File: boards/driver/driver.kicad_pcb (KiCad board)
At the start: 6 copper layers, 228.6 x 110.7 mm, 687 parts, among them J1 DIN41612_03x32_C, J2 Barrel_Jack_Switch, J3 Conn_01x24, J4 Conn_01x24, Q1 MMBT2222, Q10 MMBT2222, Q11 MMBT2222, Q12 MMBT2222, Q13 MMBT2222, Q14 MMBT2222, Q15 MMBT2222, Q16 MMBT2222, Q17 MMBT2222, Q18 MMBT2222, Q19 MMBT2222, Q2 MMBT2222, Q20 MMBT2222, Q21 MMBT2222, Q22 MMBT2222, Q23 MMBT2222, Q24 MMBT2222, Q25 MMBT2222, Q26 MMBT2222, Q27 MMBT2222, Q28 MMBT2222, Q29 MMBT2222, Q3 MMBT2222, Q30 MMBT2222, Q31 MMBT2222, Q32 MMBT2222, Q33 MMBT2222, Q34 MMBT2907, Q35 MMBT2222, Q36 MMBT2222, Q37 MMBT2907, Q38 MMBT2222, Q39 MMBT2222, Q4 MMBT2222, Q40 MMBT2907, Q41 MMBT2222, Q42 MMBT2222, Q43 MMBT2222, Q44 MMBT2907, Q45 MMBT2222, Q46 MMBT2222, Q47 MMBT2222, Q48 MMBT2907, Q49 MMBT2222, Q5 MMBT2222, Q50 MMBT2222, Q51 MMBT2222, Q52 MMBT2907, Q53 MMBT2222, Q54 MMBT2222, Q55 MMBT2222, Q56 MMBT2907, Q57 MMBT2222, Q58 MMBT2222, Q59 MMBT2222, Q6 MMBT2222, Q60 MMBT2907, Q61 MMBT2222, Q62 MMBT2222, Q63 MMBT2222, Q64 MMBT2907, Q65 MMBT2222, Q66 MMBT2907, Q67 MMBT2222, Q68 MMBT2907, Q69 MMBT2222, Q7 MMBT2222, Q70 MMBT2907, Q71 MMBT2222, Q72 MMBT2907, Q73 MMBT2222, Q74 MMBT2907, Q75 MMBT2222, Q76 MMBT2907, Q77 MMBT2222, Q78 MMBT2907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

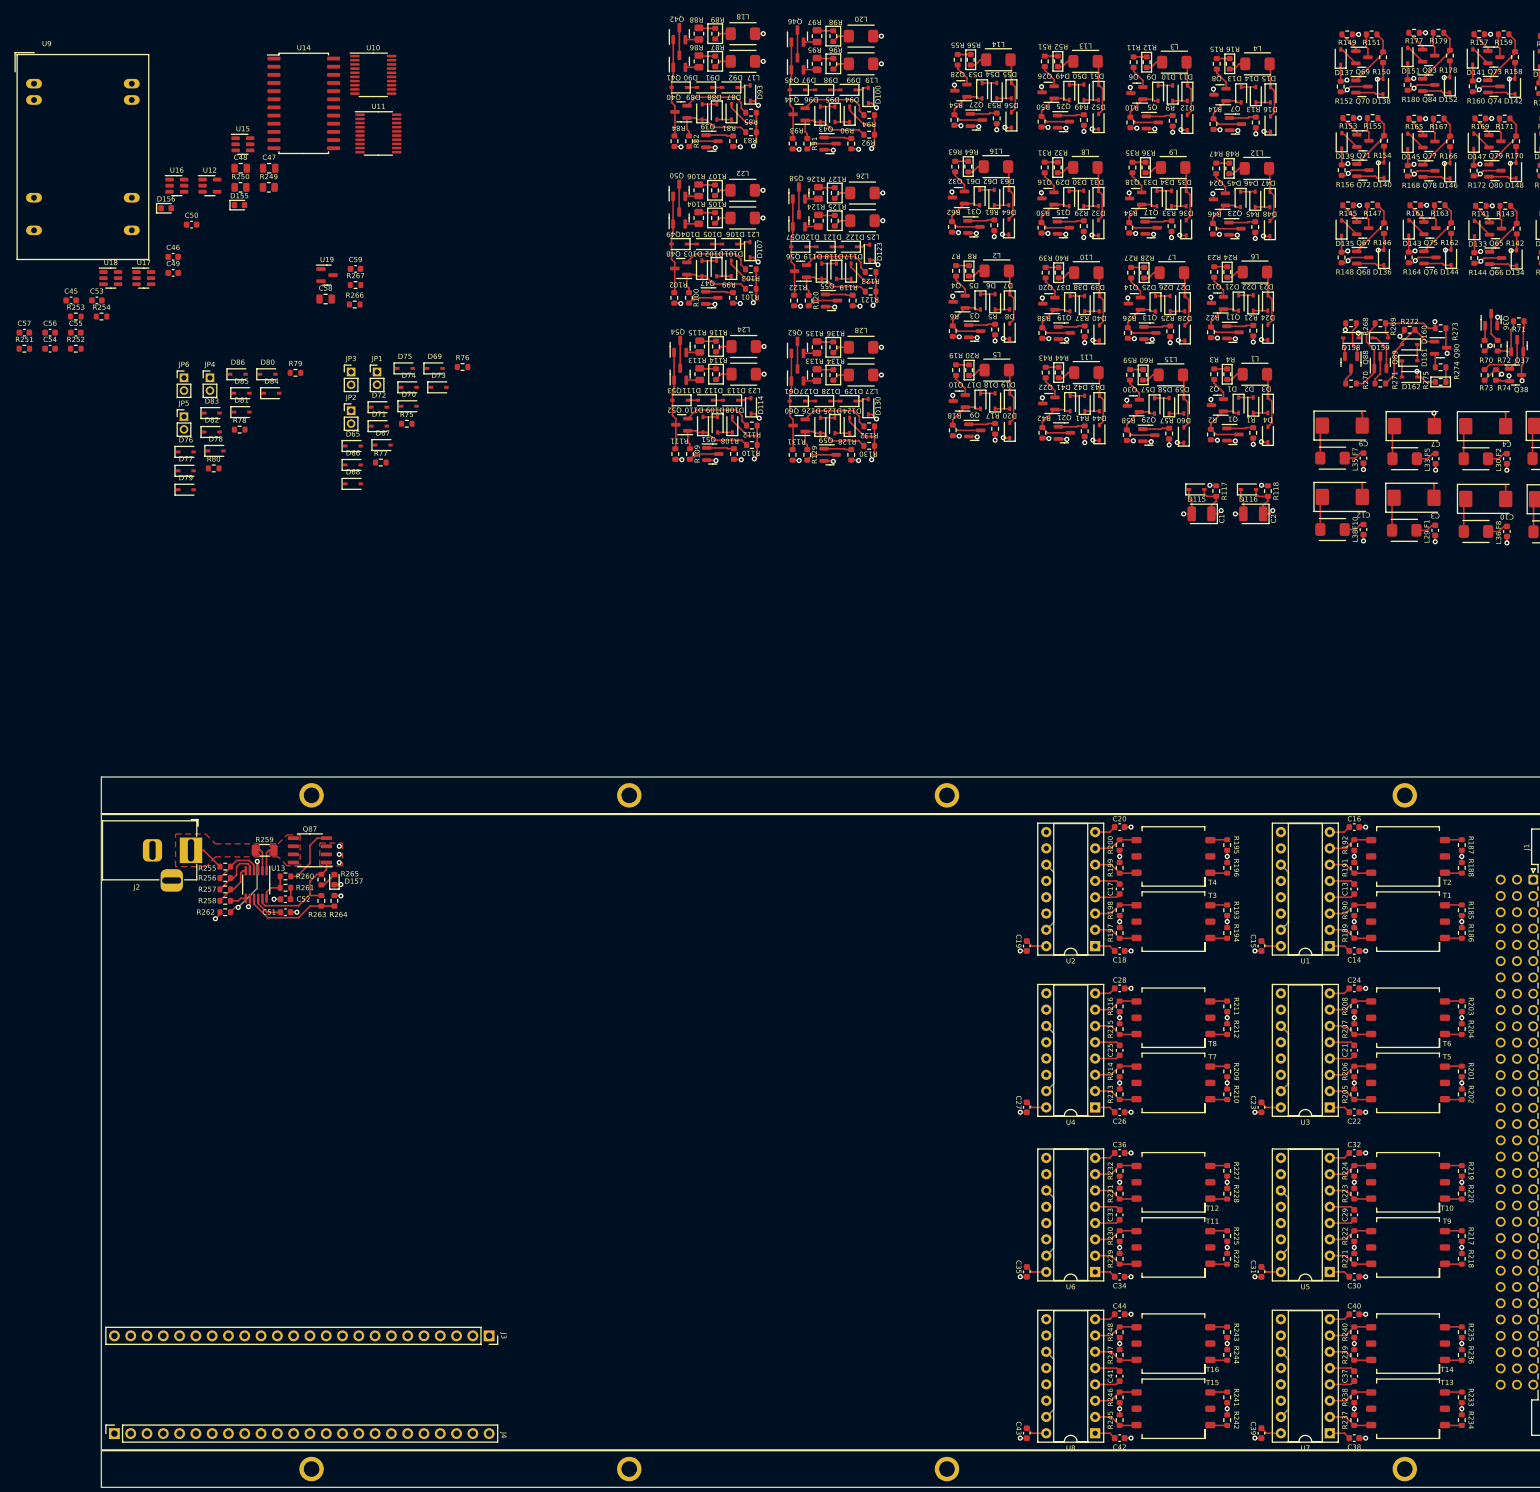
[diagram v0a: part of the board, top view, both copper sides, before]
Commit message: Driver: positioned the sense amps and laid out all of the sense wires
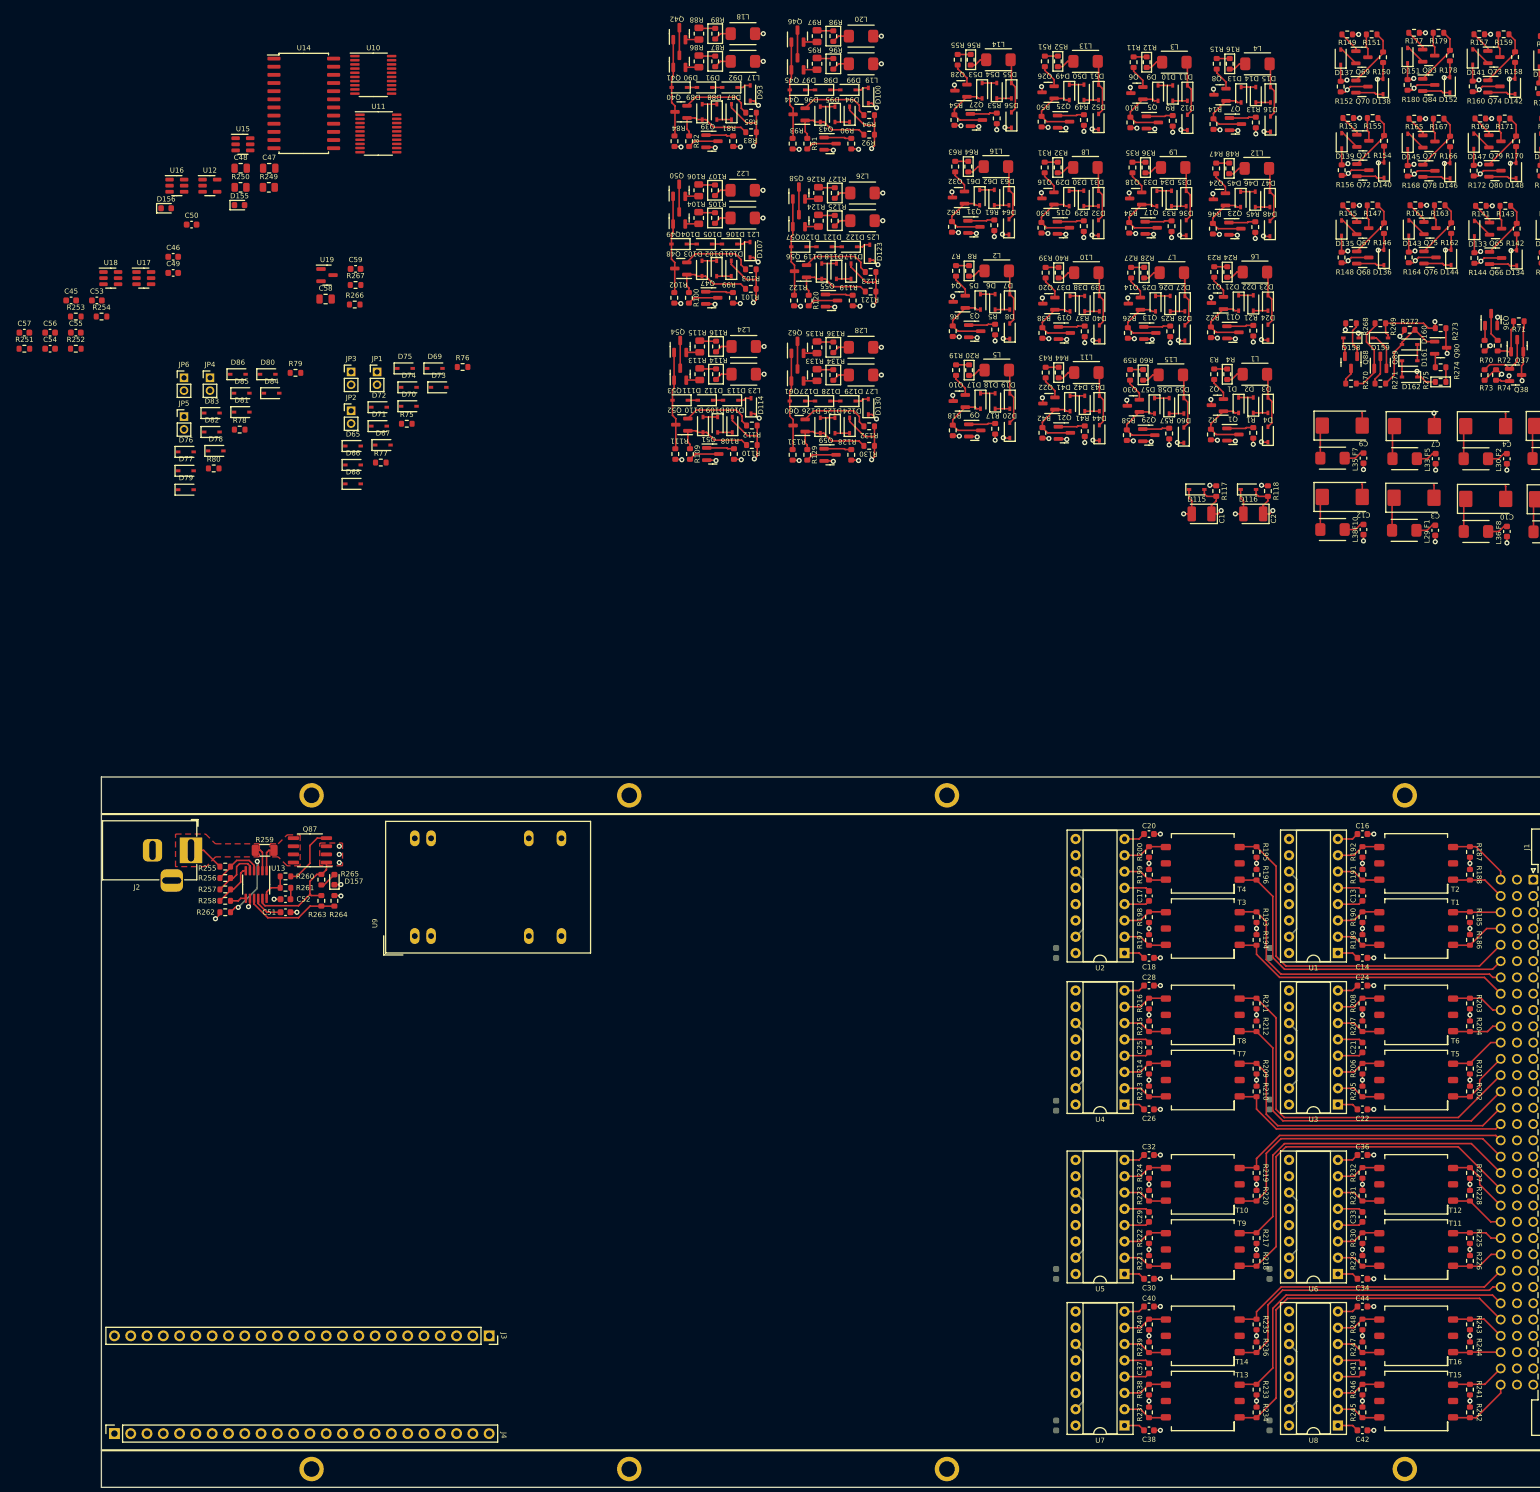
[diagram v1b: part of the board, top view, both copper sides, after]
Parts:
- C15, C19, C23, C27, C31, C35, C39, C43: moved to B.Cu
- moved U9 145.5 mm to (74.3, 50.2), turned to 90 degrees
- moved C41 37.9 mm to (222.0, 117.6)
- moved C42 37.9 mm to (222.0, 127.3)
- moved C43 37.9 mm to (207.5, 126.5)
- moved C44 37.9 mm to (222.0, 108.0)
- moved R241 37.9 mm to (238.8, 120.9)
- moved R242 37.9 mm to (238.8, 124.5)
- moved R243 37.9 mm to (238.8, 110.7)
- moved R244 37.9 mm to (238.8, 114.3)
- moved R245 37.9 mm to (222.0, 124.5)
- moved R246 37.9 mm to (222.0, 120.9)
- moved R247 37.9 mm to (222.0, 114.3)
- moved R248 37.9 mm to (222.0, 110.7)
- moved T15 37.9 mm to (230.4, 122.7)
- moved T16 37.9 mm to (230.4, 112.5)
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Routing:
- net /Connector/GAR6: track 2.66 -> 59.5 mm
- net /Connector/GBR9: track 2.66 -> 59.4 mm
- net /Connector/GAR2: track 2.66 -> 58.0 mm
- net /Connector/GBR13: track 2.66 -> 57.9 mm
- net /Connector/GBR6: track 2.66 -> 54.1 mm
- net /Connector/GAR9: track 2.66 -> 54.0 mm
- net /Connector/GBR2: track 2.66 -> 52.6 mm
- net /Connector/GAR13: track 2.66 -> 52.5 mm
- net /Connector/GAR7: track 2.66 -> 49.7 mm
- net /Connector/GBR8: track 2.66 -> 49.4 mm
- net /Connector/GAR3: track 2.66 -> 48.4 mm
- net /Connector/GBR12: track 2.66 -> 48.3 mm
- net /Connector/GBR3: track 2.66 -> 44.7 mm
- net /Connector/GAR12: track 2.66 -> 44.5 mm
- net /Connector/GBR7: track 2.66 -> 44.2 mm
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
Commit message: Driver: progress on subcircuit layout and overall placement
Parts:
- removed JP3, JP4, JP5, JP6: Jumper_2_Open, Connector_PinHeader_2.00mm:PinHeader_1x02_P2.00mm_Vertical
- C45, C46, C53, C54, C55, C56, C57, D131, D132, D133, D134, D135, D136, D137, D138, D139, D140, D141, D142, D143, D144, D145, D146, D147, D148, D149, D150, D151, D152, D153, D154, D158, D159, D160, D161, D162, Q63, Q64, Q65, Q66, Q67, Q68, Q69, Q70, Q71, Q72, Q73, Q74, Q75, Q76, Q77, Q78, Q79, Q80, Q81, Q82, Q83, Q84, Q85, Q86, Q88, Q89, Q90, R137, R138, R139, R140, R141, R142, R143, R144, R145, R146, R147, R148, R149, R150, R151, R152, R153, R154, R155, R156, R157, R158, R159, R160, R161, R162, R163, R164, R165, R166, R167, R168, R169, R170, R171, R172, R173, R174, R175, R176, R177, R178, R179, R180, R181, R182, R183, R184, R268, R269, R270, R271, R272, R273, R274, R275, U10, U11, U14, U15, U16, U17, U18: moved to B.Cu
- JP1, JP2: value Jumper_2_Open -> Conn_02x03_Odd_Even; footprint Connector_PinHeader_2.00mm:PinHeader_1x02_P2.00mm_Vertical -> Connector_PinHeader_2.00mm:PinHeader_2x03_P2.00mm_Vertical
- moved R78 324.7 mm to (366.0, 31.2), turned to 90 degrees
- moved R80 323.6 mm to (362.0, 31.2), turned to 90 degrees
- moved D76 318.5 mm to (352.6, 28.2), turned to -90 degrees
- moved D83 318.1 mm to (355.1, 28.2), turned to -90 degrees
- moved D86 317.8 mm to (357.7, 28.2), turned to -90 degrees
- moved R79 315.9 mm to (364.0, 31.2), turned to 90 degrees
- moved D82 309.1 mm to (346.5, 28.2), turned to -90 degrees
- moved JP2 308.9 mm to (366.0, 34.8), turned to -90 degrees
- moved D85 308.2 mm to (349.0, 28.2), turned to -90 degrees
- moved D78 303.0 mm to (341.4, 28.2), turned to -90 degrees
- moved D80 299.9 mm to (343.9, 28.2), turned to -90 degrees
- moved D79 298.8 mm to (333.5, 28.2), turned to -90 degrees
- moved D77 296.7 mm to (331.0, 28.2), turned to -90 degrees
- moved D81 294.9 mm to (336.1, 28.2), turned to -90 degrees
- moved D84 293.4 mm to (338.6, 28.2), turned to -90 degrees
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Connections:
- net Net-(C49-Pad2) renamed /FPGA and Power/5V_FPGA
- JP1 pad 1: /Connector/XRST4 -> Net-(JP1-Pad1)
- JP1 pad 2: Net-(JP1-Pad2) -> /Connector/XRST4
- JP2 pad 1: /Connector/XRST3 -> Net-(JP2-Pad1)
- JP2 pad 2: Net-(JP2-Pad2) -> /Connector/XRST2
- R75 pad 1: Net-(JP1-Pad2) -> Net-(JP1-Pad1)
- R76 pad 1: Net-(JP2-Pad2) -> Net-(JP1-Pad3)
- R77 pad 1: Net-(JP3-Pad2) -> Net-(JP1-Pad5)
- R78 pad 1: Net-(JP4-Pad2) -> Net-(JP2-Pad1)
- R79 pad 1: Net-(JP5-Pad2) -> Net-(JP2-Pad3)
- R80 pad 1: Net-(JP6-Pad2) -> Net-(JP2-Pad5)
- U1 pad 12: /FPGA and Power/SA2 -> /FPGA and Power/SA1
- U1 pad 14: /FPGA and Power/SA1 -> /FPGA and Power/SA15
- U2 pad 12: /FPGA and Power/SA4 -> /FPGA and Power/SA3
- U2 pad 14: /FPGA and Power/SA3 -> /FPGA and Power/SA2
- U3 pad 12: /FPGA and Power/SA6 -> /FPGA and Power/SA5
- U3 pad 14: /FPGA and Power/SA5 -> /FPGA and Power/SA4
- U4 pad 12: /FPGA and Power/SA8 -> /FPGA and Power/SA7
- U4 pad 14: /FPGA and Power/SA7 -> /FPGA and Power/SA6
- U5 pad 12: /FPGA and Power/SA10 -> /FPGA and Power/SA9
- U5 pad 14: /FPGA and Power/SA9 -> /FPGA and Power/SA8
- U6 pad 12: /FPGA and Power/SA12 -> /FPGA and Power/SA11
- U6 pad 14: /FPGA and Power/SA11 -> /FPGA and Power/SA10
- U7 pad 12: /FPGA and Power/SA14 -> /FPGA and Power/SA13
- U7 pad 14: /FPGA and Power/SA13 -> /FPGA and Power/SA12
- U8 pad 14: /FPGA and Power/SA15 -> /FPGA and Power/SA14
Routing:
- net +3V3: track 0.00 -> 20.5 mm, vias 0 -> 6
- net /Rope Drivers/BPLMY2: track 5.21 -> 16.5 mm
- net /Rope Drivers/BPLMY1: track 5.21 -> 16.5 mm
- net /FPGA and Power/5V_FPGA: track 0.00 -> 10.5 mm
- net GND: track 220.8 -> 229.4 mm, vias 98 -> 110
- net /Rope Drivers/BPLMY3: track 5.21 -> 13.3 mm
- net Net-(JP2-Pad5): track 0.00 -> 2.76 mm
- net Net-(JP2-Pad1): track 0.00 -> 2.76 mm
- net Net-(JP2-Pad3): track 0.00 -> 2.75 mm
- net /FPGA and Power/ADC_5V: track 0.00 -> 2.73 mm
- net /FPGA and Power/ADC_14V: track 0.00 -> 2.73 mm
- net /Connector/SETRN2: track 0.00 -> 1.09 mm, vias 0 -> 1
- net /Connector/RSTRD2: track 0.00 -> 1.09 mm, vias 0 -> 1
- net /Connector/RSTRD1: track 0.00 -> 1.09 mm, vias 0 -> 1
- net /Connector/RFD8: track 0.00 -> 1.09 mm, vias 0 -> 1
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- added copper zone on F.Cu, net +3V3
- added copper zone on F.Cu, net /FPGA and Power/5V_FPGA
- added copper zone on F.Cu, net GND

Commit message: Driver: 3.3V section is now laid out, contained entirely beneath the FPGA daughter board
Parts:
- C45, C54, C55, C56, C57, U11, U15, U16, U17, U18: moved to F.Cu
- moved U15 33.1 mm to (30.2, 122.7)
- moved C54 27.5 mm to (33.0, 122.7)
- moved C53 25.8 mm to (70.5, 118.4)
- moved U14 23.8 mm to (61.6, 120.1)
- moved U16 21.9 mm to (35.8, 122.7)
- moved C55 16.4 mm to (38.6, 122.7)
- moved U10 15.7 mm to (83.8, 120.1), turned to 180 degrees
- moved U11 15.5 mm to (83.8, 120.1), turned to 180 degrees
- moved C45 11.8 mm to (82.0, 124.7), turned to 180 degrees
- moved C46 11.7 mm to (82.0, 115.6), turned to 180 degrees
- moved U17 10.8 mm to (41.4, 122.7)
- moved C57 6.35 mm to (49.8, 122.7)
- moved C56 5.38 mm to (44.2, 122.7)
- moved U18 1.85 mm to (47.0, 122.7)
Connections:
- J3 pad 1: /FPGA and Power/SAF1 -> /FPGA and Power/SAF13
- J3 pad 10: /FPGA and Power/SAF10 -> /FPGA and Power/STRA2
- J3 pad 11: /FPGA and Power/SAF11 -> /FPGA and Power/RESET2
- J3 pad 12: /FPGA and Power/SAF12 -> /FPGA and Power/RESET3
- J3 pad 13: /FPGA and Power/SAF13 -> /FPGA and Power/ROPER
- J3 pad 14: /FPGA and Power/SAF14 -> /FPGA and Power/SET1
- J3 pad 17: /FPGA and Power/SAF15 -> /FPGA and Power/EN_14V
- J3 pad 18: /FPGA and Power/SAF16 -> /FPGA and Power/PG_14V
- J3 pad 2: /FPGA and Power/SAF2 -> /FPGA and Power/SAF14
- J3 pad 3: /FPGA and Power/SAF3 -> /FPGA and Power/SAF15
- J3 pad 4: /FPGA and Power/SAF4 -> /FPGA and Power/SAF16
- J3 pad 5: /FPGA and Power/SAF5 -> /FPGA and Power/SAF1
- J3 pad 6: /FPGA and Power/SAF6 -> /FPGA and Power/SAF2
- J3 pad 7: /FPGA and Power/SAF7 -> /FPGA and Power/SAF3
- J3 pad 8: /FPGA and Power/SAF8 -> /FPGA and Power/SAF4
- J3 pad 9: /FPGA and Power/SAF9 -> /FPGA and Power/STRA3
- J4 pad 10: /FPGA and Power/IL6 -> unconnected-(J4-Pad10)
- J4 pad 11: /FPGA and Power/IL5 -> /FPGA and Power/RESET4
- J4 pad 12: /FPGA and Power/IL4 -> /FPGA and Power/RESET1
- J4 pad 13: /FPGA and Power/IL3 -> /FPGA and Power/SET2
- J4 pad 14: /FPGA and Power/IL2 -> /FPGA and Power/IHENV
- J4 pad 15: /FPGA and Power/IL1 -> /FPGA and Power/STRA1
- J4 pad 16: /FPGA and Power/RESET4 -> /FPGA and Power/STRA0
- J4 pad 17: /FPGA and Power/RESET3 -> /FPGA and Power/SAF12
- J4 pad 18: /FPGA and Power/RESET2 -> /FPGA and Power/SAF11
- J4 pad 19: /FPGA and Power/RESET1 -> /FPGA and Power/SAF10
- J4 pad 2: unconnected-(J4-Pad2) -> /FPGA and Power/IL1
- J4 pad 20: /FPGA and Power/SET2 -> /FPGA and Power/SAF9
- J4 pad 21: /FPGA and Power/SET1 -> /FPGA and Power/SAF8
- J4 pad 22: /FPGA and Power/ROPER -> /FPGA and Power/SAF7
- J4 pad 23: /FPGA and Power/PG_14V -> /FPGA and Power/SAF6
- J4 pad 24: /FPGA and Power/EN_14V -> /FPGA and Power/SAF5
- J4 pad 3: /FPGA and Power/STRA3 -> /FPGA and Power/IL2
- J4 pad 4: /FPGA and Power/STRA2 -> /FPGA and Power/IL3
- J4 pad 5: /FPGA and Power/STRA1 -> /FPGA and Power/IL4
- J4 pad 6: /FPGA and Power/STRA0 -> /FPGA and Power/IL5
- J4 pad 7: /FPGA and Power/IHENV -> /FPGA and Power/IL6
- J4 pad 8: /FPGA and Power/IL8 -> /FPGA and Power/IL7
- J4 pad 9: /FPGA and Power/IL7 -> /FPGA and Power/IL8
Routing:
- net GND: track 229.4 -> 254.6 mm, vias 110 -> 117
- net +3V3: track 20.5 -> 44.2 mm, vias 6 -> 10
- net /FPGA and Power/SAF12: track 0.00 -> 16.2 mm
- net /FPGA and Power/SAF4: track 0.00 -> 16.2 mm
- net /FPGA and Power/SAF11: track 0.00 -> 13.4 mm
- net /FPGA and Power/SAF3: track 0.00 -> 13.4 mm
- net /FPGA and Power/SAF2: track 0.00 -> 10.6 mm
- net /FPGA and Power/SAF10: track 0.00 -> 10.6 mm
- net /FPGA and Power/SAF13: track 0.00 -> 9.56 mm
- net /FPGA and Power/SAF5: track 0.00 -> 9.56 mm
- net /FPGA and Power/SAF9: track 0.00 -> 8.79 mm
- net /FPGA and Power/SAF1: track 0.00 -> 8.79 mm
- net /FPGA and Power/SAF6: track 0.00 -> 7.81 mm
- net /FPGA and Power/SAF14: track 0.00 -> 7.81 mm
- net /FPGA and Power/SAF15: track 0.00 -> 7.37 mm
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- added copper zone on In4.Cu, net +3V3
